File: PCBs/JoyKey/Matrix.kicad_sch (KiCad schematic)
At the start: 20 parts, among them J5 Top Trigger 1, J6 Top Trigger 2, J7 Extra Trigger, SW2 SW_Push_45deg, SW3 SW_Push_45deg, SW4 SW_Push_45deg, SW5 SW_Push_45deg, SW6 SW_Push_45deg, SW7 SW_Push_45deg

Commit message: Updated BOM with LCSC parts
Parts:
- D1, D11, D12, D14, D15, D16, D17, D2, D3, D4, D9: LCSC (none) -> C2128
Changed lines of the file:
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@@
+			)
+		)
+		(property "LCSC" "C2128"
+			(at 135.89 119.38 90)
+			(effects
+				(font
+					(size 1.27 1.27)
+				)
+				(hide yes)
 			)
 		)
@@
 			)
 		)
+		(property "LCSC" "C2128"
+			(at 120.65 119.38 90)
+			(effects
+				(font
+					(size 1.27 1.27)
+				)
+				(hide yes)
+			)
+		)
 		(pin "1"
 		)
@@
 			)
 		)
+		(property "LCSC" "C2128"
+			(at 120.65 74.93 90)
+			(effects
+				(font
+					(size 1.27 1.27)
+				)
+				(hide yes)
+			)
+		)
 		(pin "1"
 		)
@@
 			)
 		)
+		(property "LCSC" "C2128"
+			(at 120.65 97.79 90)
+			(effects
+				(font
+					(size 1.27 1.27)
+				)
+				(hide yes)
+			)
+		)
 		(pin "1"
 		)
@@
 			)
 		)
+		(property "LCSC" "C2128"
+			(at 163.83 74.93 90)
+			(effects
+				(font
+					(size 1.27 1.27)
+				)
+				(hide yes)
+			)
+		)
 		(pin "1"
 		)
@@
 			)
 		)
+		(property "LCSC" "C2128"
+			(at 135.89 97.79 90)
+			(effects
+				(font
+					(size 1.27 1.27)
+				)
+				(hide yes)
+			)
+		)
 		(pin "1"
 		)
@@
 			)
 		)
+		(property "LCSC" "C2128"
+			(at 149.86 74.93 90)
+			(effects
+				(font
+					(size 1.27 1.27)
+				)
+				(hide yes)
+			)
+		)
 		(pin "1"
 		)
@@
 			)
 		)
+		(property "LCSC" "C2128"
+			(at 135.89 74.93 90)
+			(effects
+				(font
+					(size 1.27 1.27)
+				)
+				(hide yes)
+			)
+		)
 		(pin "1"
 		)
@@
 			)
 		)
+		(property "LCSC" "C2128"
+			(at 163.83 119.38 90)
+			(effects
+				(font
+					(size 1.27 1.27)
+				)
+				(hide yes)
+			)
+		)
 		(pin "1"
 		)
@@
 			)
 		)
+		(property "LCSC" "C2128"
+			(at 149.86 119.38 90)
+			(effects
+				(font
+					(size 1.27 1.27)
+				)
+				(hide yes)
+			)
+		)
 		(pin "1"
 		)
@@
 			(effects
 				(font
+					(size 1.27 1.27)
+				)
+				(hide yes)
+			)
+		)
+		(property "LCSC" "C2128"
+			(at 149.86 99.06 90)
+			(effects
+				(font

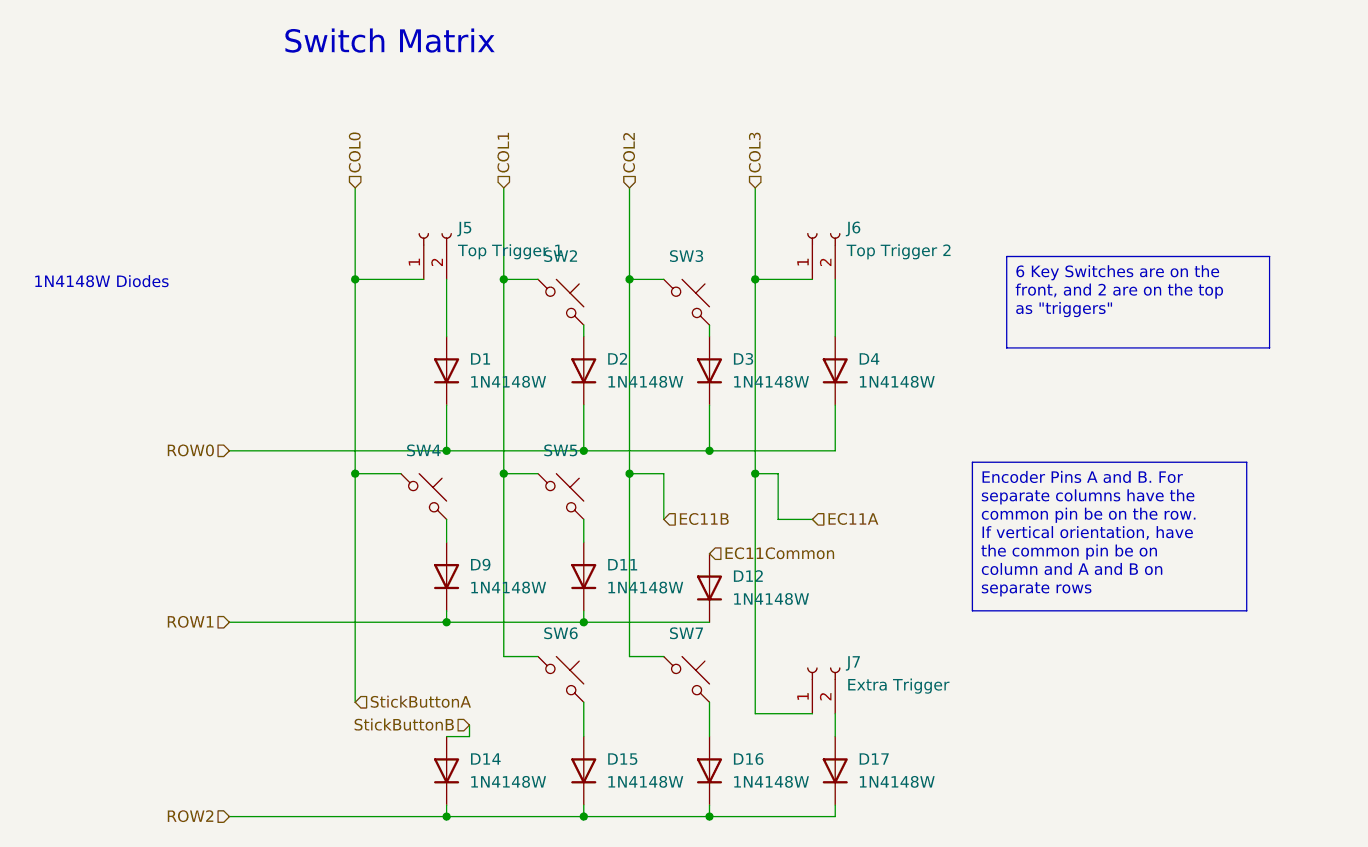
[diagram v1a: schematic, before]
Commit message: Switched encoder to Alps SRBE110301 in sch
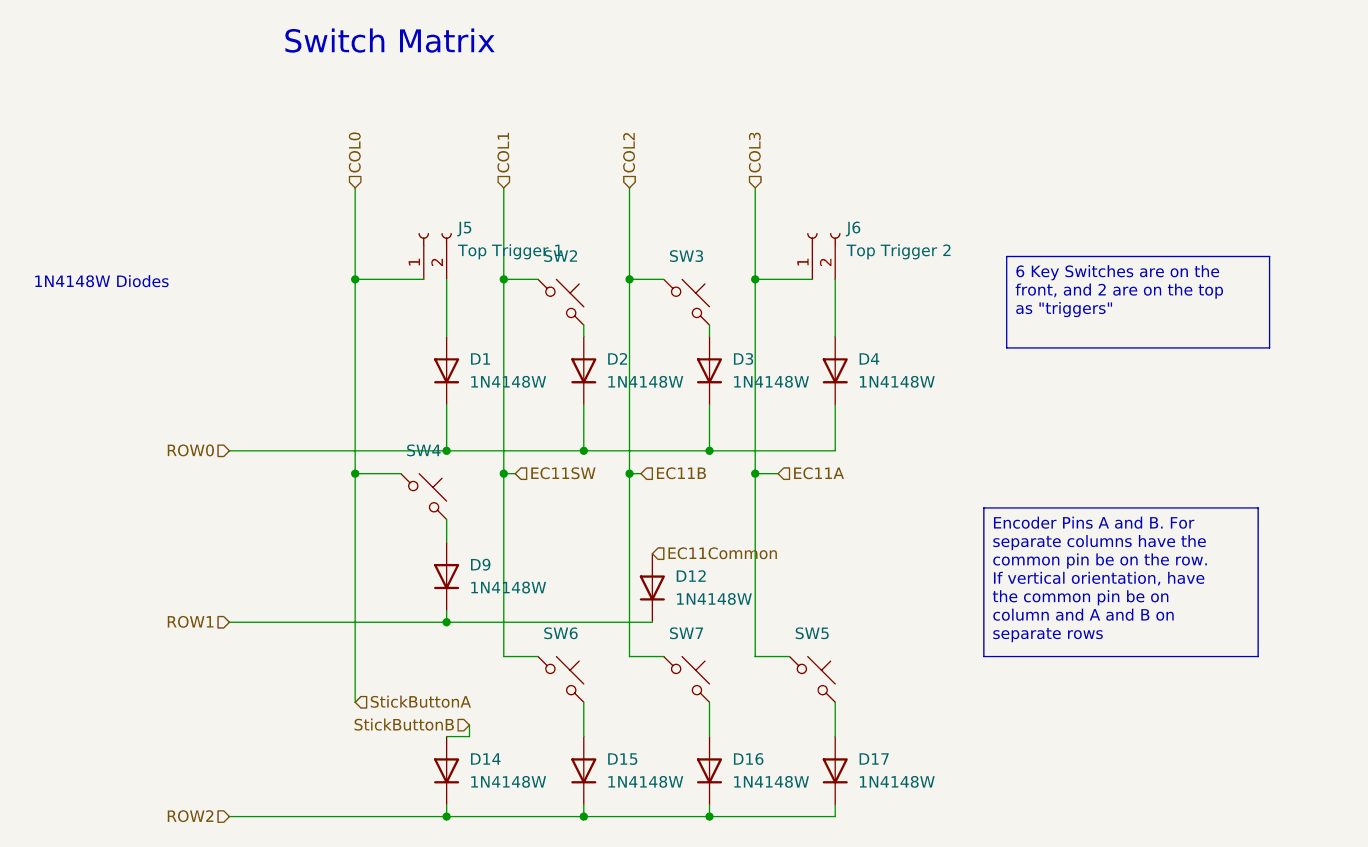
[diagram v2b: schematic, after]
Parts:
- removed D11: 1N4148W, Diode_SMD:Nexperia_CFP3_SOD-123W, symbol Device:D
- removed J7: Extra Trigger, Connector_PinHeader_2.54mm:PinHeader_1x02_P2.54mm_Vertical, symbol Connector:Conn_01x02_Socket
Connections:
- net COL1: no longer SW5.1
- net COL3: now also SW5.1
- net at SW5.2: now also D17.2 (A)
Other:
- moved on the sheet: D12, SW5

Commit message: Updated to Vertical matrix orientation of encoder
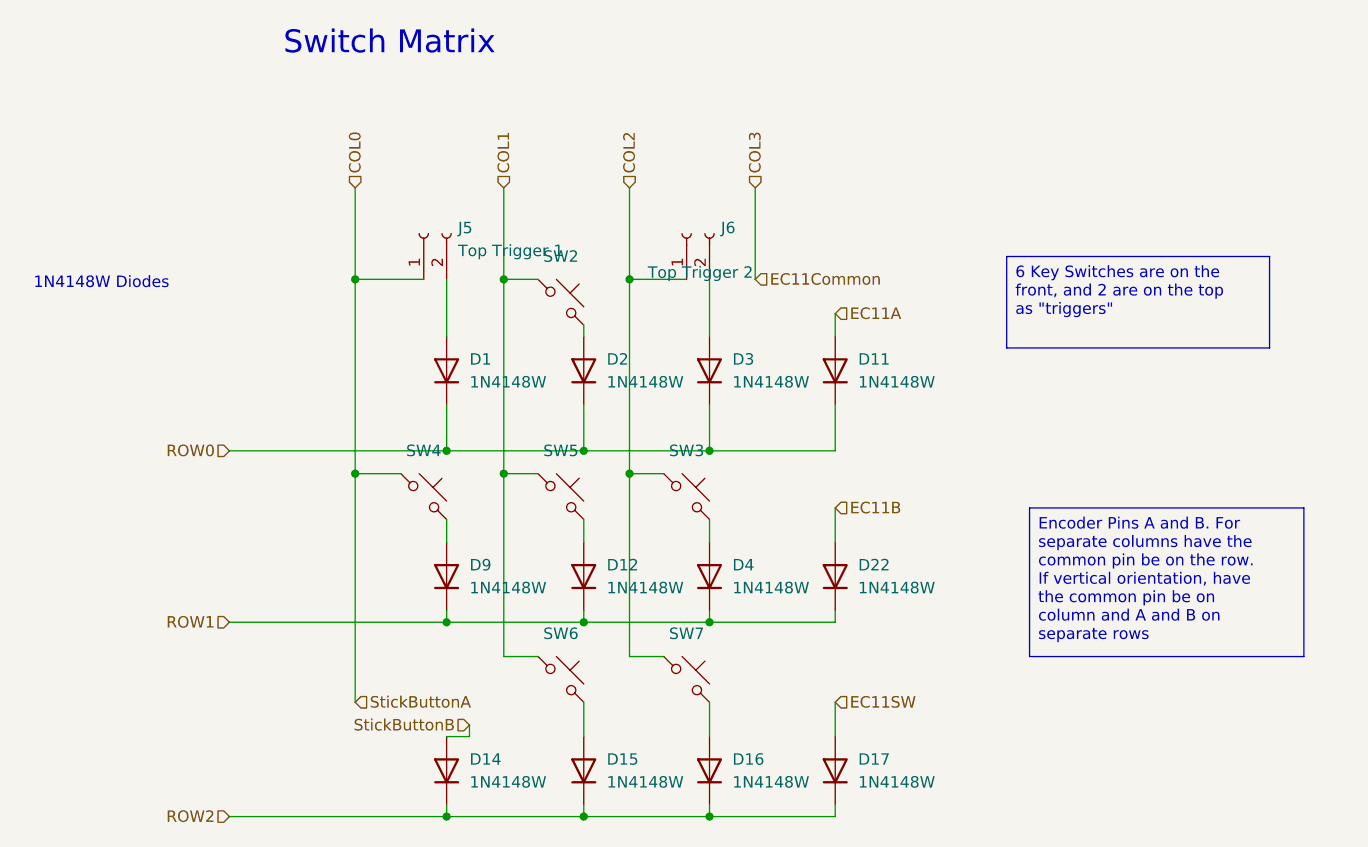
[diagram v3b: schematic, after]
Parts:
- added D11, D22: 1N4148W, Diode_SMD:Nexperia_CFP3_SOD-123W, symbol Device:D
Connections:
- net EC11Common is gone; now on an unnamed net: D12.2 (A)
- net COL1: now also SW5.1
- net COL2: now also J6.1 (Pin_1)
- net COL3: no longer J6.1 (Pin_1), SW5.1
- net ROW0: now also D11.1 (K); no longer D4.1 (K)
- net ROW1: now also D4.1 (K), D22.1 (K)
- net at SW3.2: now also D4.2 (A); no longer D3.2 (A)
- net at J6.2 (Pin_2): now also D3.2 (A); no longer D4.2 (A)
- net at SW5.2: no longer D17.2 (A)
- new net EC11A: D11.2 (A)
- new net EC11B: D22.2 (A)
- new net EC11SW: D17.2 (A)
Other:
- moved on the sheet: D12, D4, J6, SW3, SW5
